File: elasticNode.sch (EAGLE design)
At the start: 138 parts, among them J1 FEMALE_HEADER_5X2, J10 FEMALE_HEADER_10X2, J11 USB_CONNMICRO_SMT, J2 FEMALE_HEADER_5X2, J3 ISP_CONN_6PIN, J4 FEMALE_HEADER_2X1, J5 JUMPER, J6 ISP_CONN_6PIN, J7 JUMPER, J8 USB_CONNMICRO_SMT, J9 JTAG_CONN_6PINSMT, M1 SISS23DN, M2 SISS23DN, M3 SISS23DN, M4 SISS23DN, U1 AT90USB128, U10 PAC1720, U11 LTC3419DFN, U12 LTC3419DFN, U2 MRF24J40MA, U3 ATMEGA32U4QFN, U4 IS66WV51216EALL, U5 SPARTAN7-LX15, U6 SST26VF032BWDFN, U7 PAC1720, U8 PAC1720, U9 PAC1720, X1 8MHz, X2 8MHz, X3 100MHz, X4 50MHz, X5 32MHz

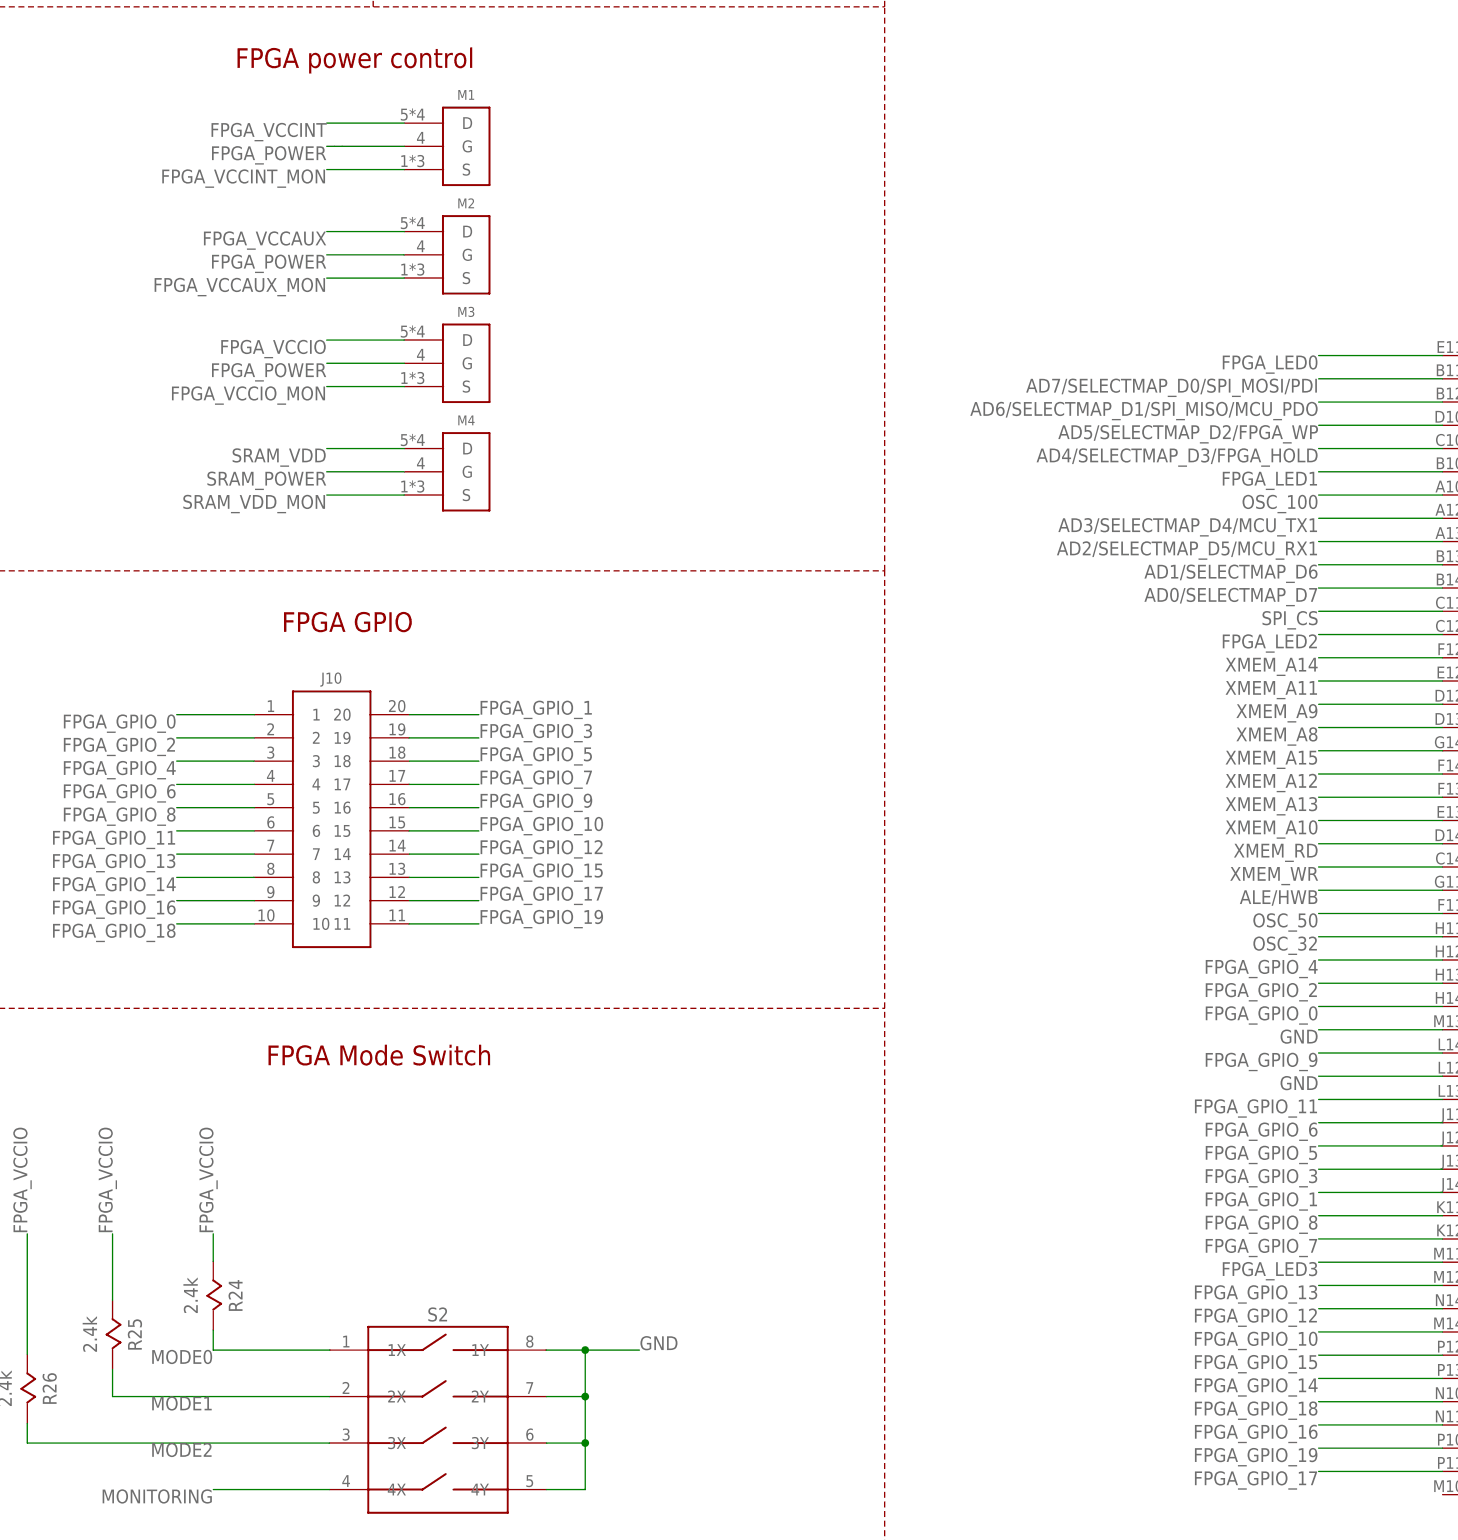
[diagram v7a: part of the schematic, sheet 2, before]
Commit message: Modified the footprint of the FPGA and MCU.
Rechecked the board again.
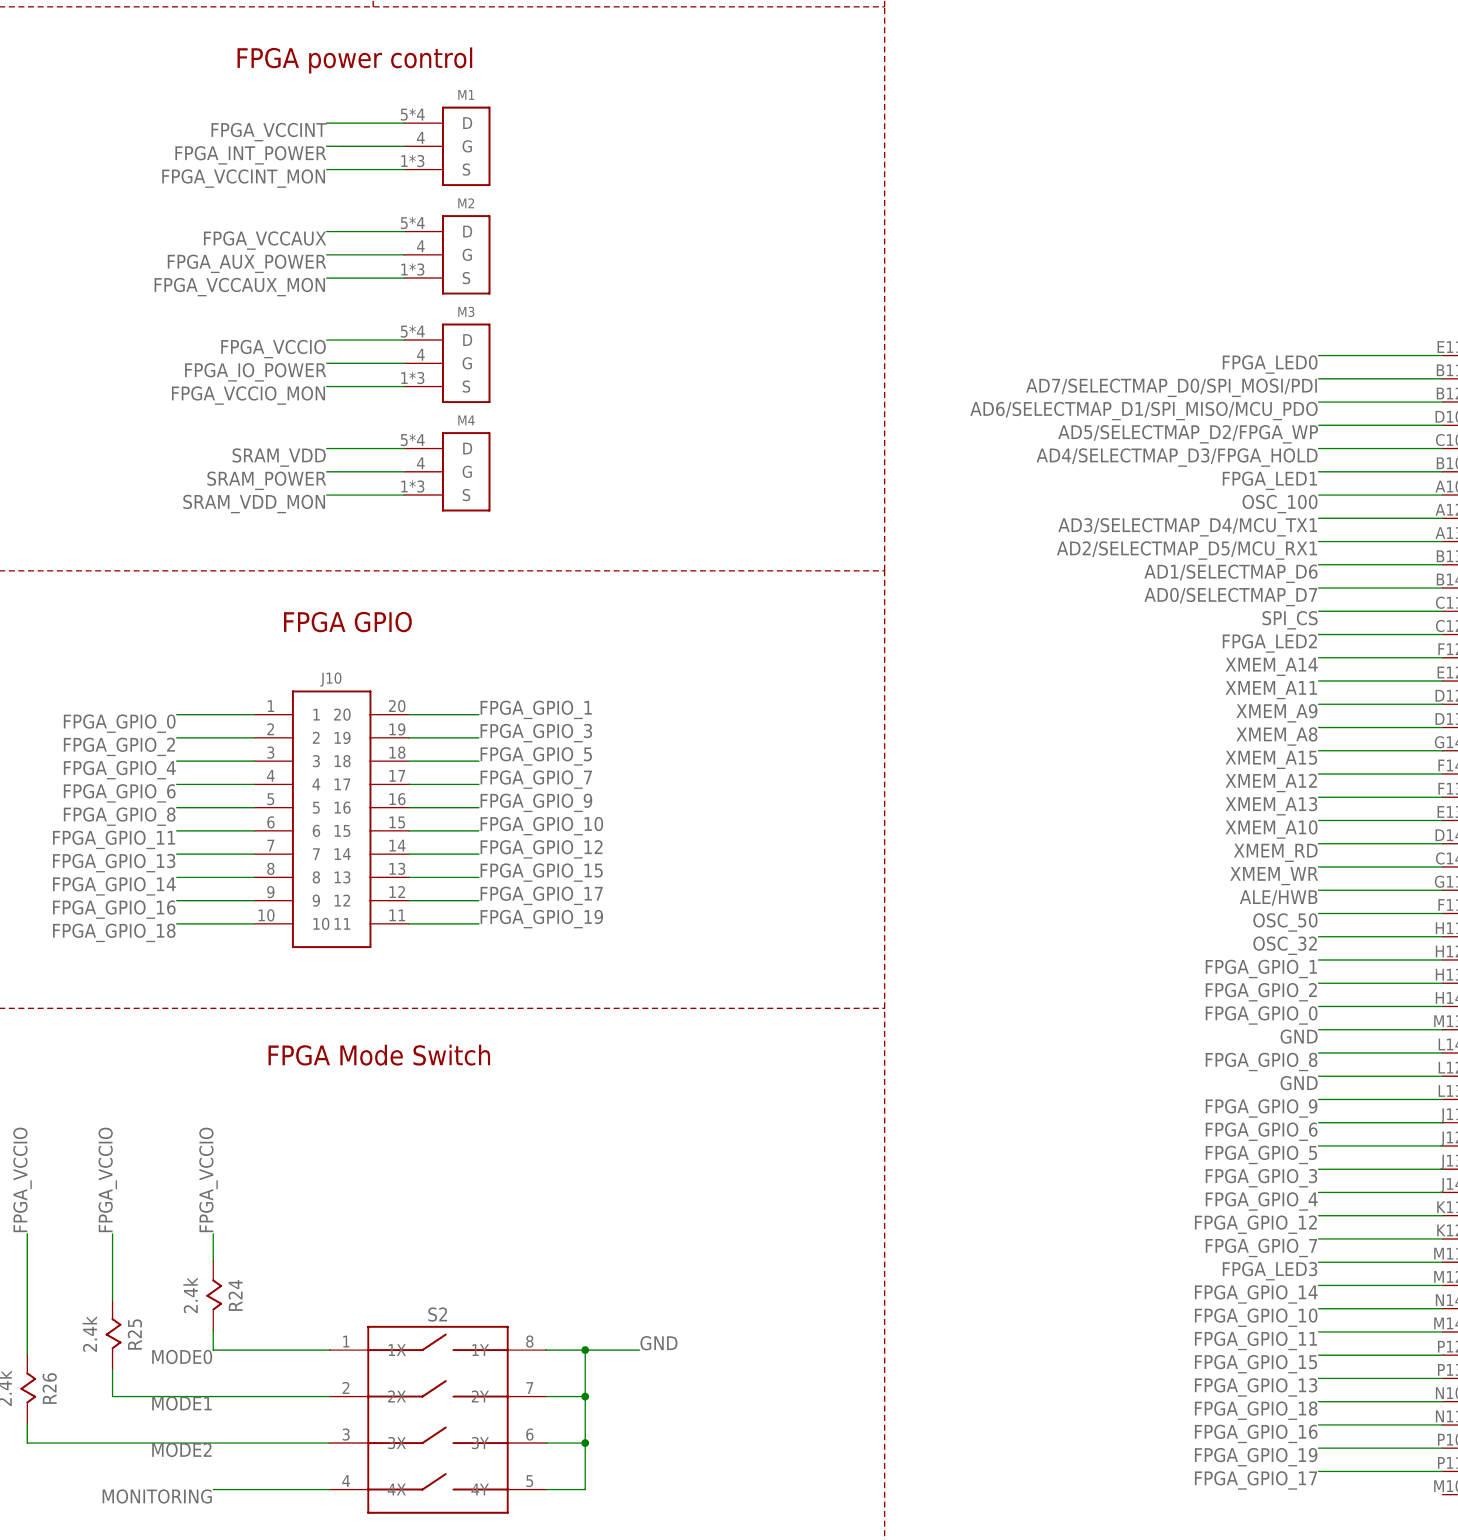
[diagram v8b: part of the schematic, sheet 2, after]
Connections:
- removed net FPGA_POWER: M1.G, M2.G, M3.G, U1.(INT4/TOSC1)PE4
- new net FPGA_AUX_POWER: M2.G, U1.(INT4/TOSC1)PE4
- new net FPGA_INT_POWER: M1.G, U1.(SS/PCINT0)PB0
- new net FPGA_IO_POWER: M3.G, U1.(INT.7/AIN.1/UVCON)PE7
- net FPGA_GPIO_1: now also U5.IO_L13N_T2_MRCC_14; no longer U5.IO_L18N_T2_D27_14
- net FPGA_GPIO_10: now also U5.IO_L21P_T3_DQS_14; no longer U5.IO_L21N_T3_DQS_D22_14
- net FPGA_GPIO_11: now also U5.IO_L21N_T3_DQS_D22_14; no longer U5.IO_L16N_T2_D31_14
- net FPGA_GPIO_12: now also U5.IO_L19P_T3_D26_14; no longer U5.IO_L21P_T3_DQS_14
- net FPGA_GPIO_13: now also U5.IO_L22N_T3_D20_14; no longer U5.IO_L20N_T3_D23_14
- net FPGA_GPIO_14: now also U5.IO_L20N_T3_D23_14; no longer U5.IO_L22N_T3_D20_14
- net FPGA_GPIO_4: now also U5.IO_L18N_T2_D27_14; no longer U5.IO_L13N_T2_MRCC_14
- net FPGA_GPIO_8: now also U5.IO_L15N_T2_DQS_DOUT_CSO_B_14; no longer U5.IO_L19P_T3_D26_14
- net FPGA_GPIO_9: now also U5.IO_L16N_T2_D31_14; no longer U5.IO_L15N_T2_DQS_DOUT_CSO_B_14
